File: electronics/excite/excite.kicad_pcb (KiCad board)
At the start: 2 copper layers, 40.9 x 45.1 mm, 22 parts, among them J1 Conn_02x06_Counter_Clockwise, J2 TBP02R2-381-02BE, J3 PJ-002A, Q1 DMP6023LE-13, U1 AP63203WU-7, U2 MIC29150-12WU-TR

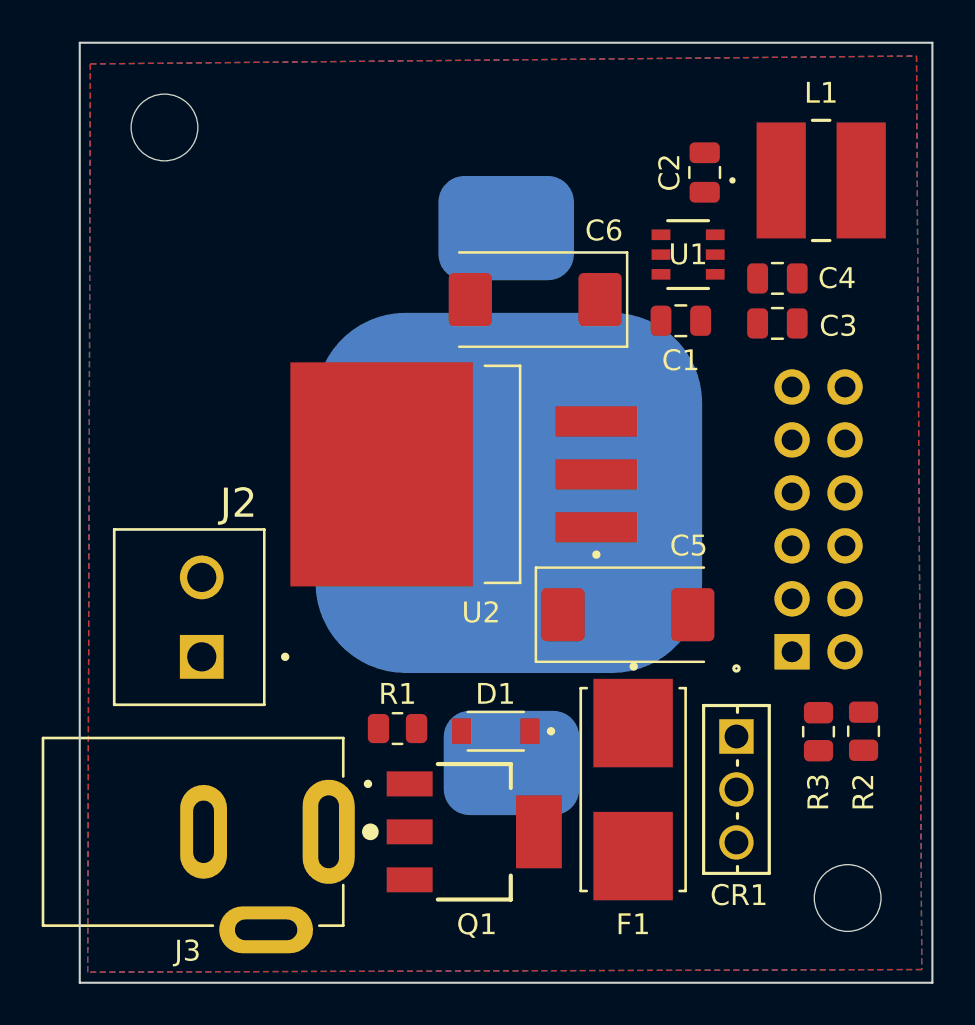
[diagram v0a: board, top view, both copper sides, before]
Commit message: working on cuvette mount and finished routing both pcbs
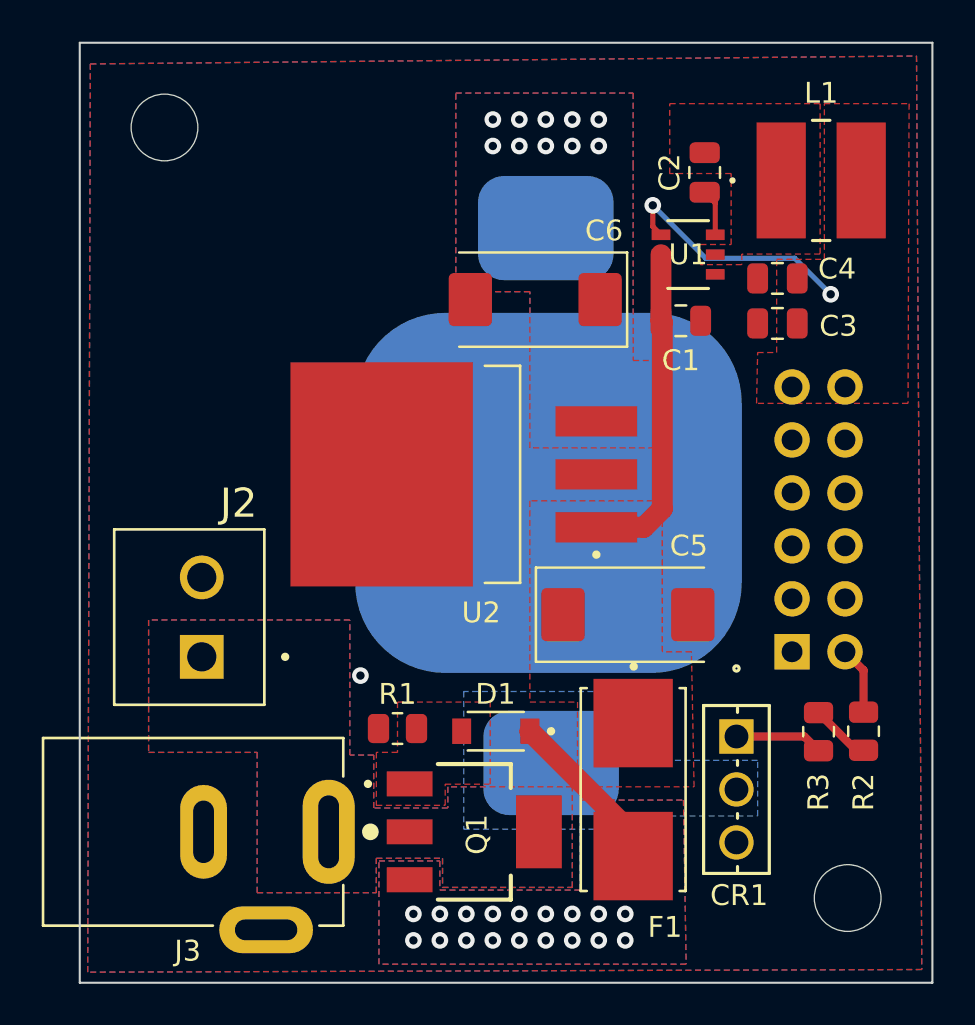
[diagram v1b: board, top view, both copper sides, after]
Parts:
- moved U3 1.90 mm to (191.5, 80.1)
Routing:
- net VDD: track 0.00 -> 15.7 mm
- net +3.3V: track 0.00 -> 11.9 mm, vias 0 -> 2
- net Net-(D1-K): track 0.00 -> 8.04 mm, vias 0 -> 18
- net Net-(CR1-Pad1): track 0.00 -> 4.22 mm
- net /FLU_EXCITE/EXCITE_EN: track 0.00 -> 3.27 mm
- net Net-(R2-Pad2): track 0.00 -> 2.91 mm
- net Net-(U1-BST): track 0.00 -> 2.25 mm
- net Net-(U2-VOUT): vias 0 -> 10
- net GND: vias 0 -> 1
- added copper zone on F.Cu, net +3.3V
- added copper zone on B.Cu, net Net-(CR1-Pad2)
- added copper zone on F.Cu, net Net-(D1-A)
- added copper zone on B.Cu, net Net-(D1-K)
- added copper zone on F.Cu, net Net-(D1-K)
- added copper zone on B.Cu, net Net-(J2-Pad1)
- added copper zone on F.Cu, net Net-(J2-Pad1)
- added copper zone on F.Cu, net Net-(U1-SW)
- added copper zone on B.Cu, net Net-(U2-VOUT)
- added copper zone on F.Cu, net Net-(U2-VOUT)
- added copper zone on F.Cu, net VDD
